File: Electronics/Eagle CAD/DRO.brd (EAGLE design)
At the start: 52.1 x 98 mm, 40 parts, among them J1 USB_MINI-B-MICRO-B_FCI, J10 CONN-4-2.54X1-RA, J11 USB-A-SHIELD, J12 CONN-8-2.54X2, J13 CONN-10-ARM, J14 CONN-40, J2 DE-9F-V, J3 DE-9F-V, J4 DE-9F-V, J5 DE-9F-V, J6 CONN-14-BIDI, J7 CONN-14-BIDI, J8 CONN-14-BIDI, J9 CONN-14-BIDI, SW1 SWITCH-SPDT-MINI-RA-SHORT, U1 74LCX14, U2 MIC5504-3.3, U3 SAMD21J17D, U4 74LCX14

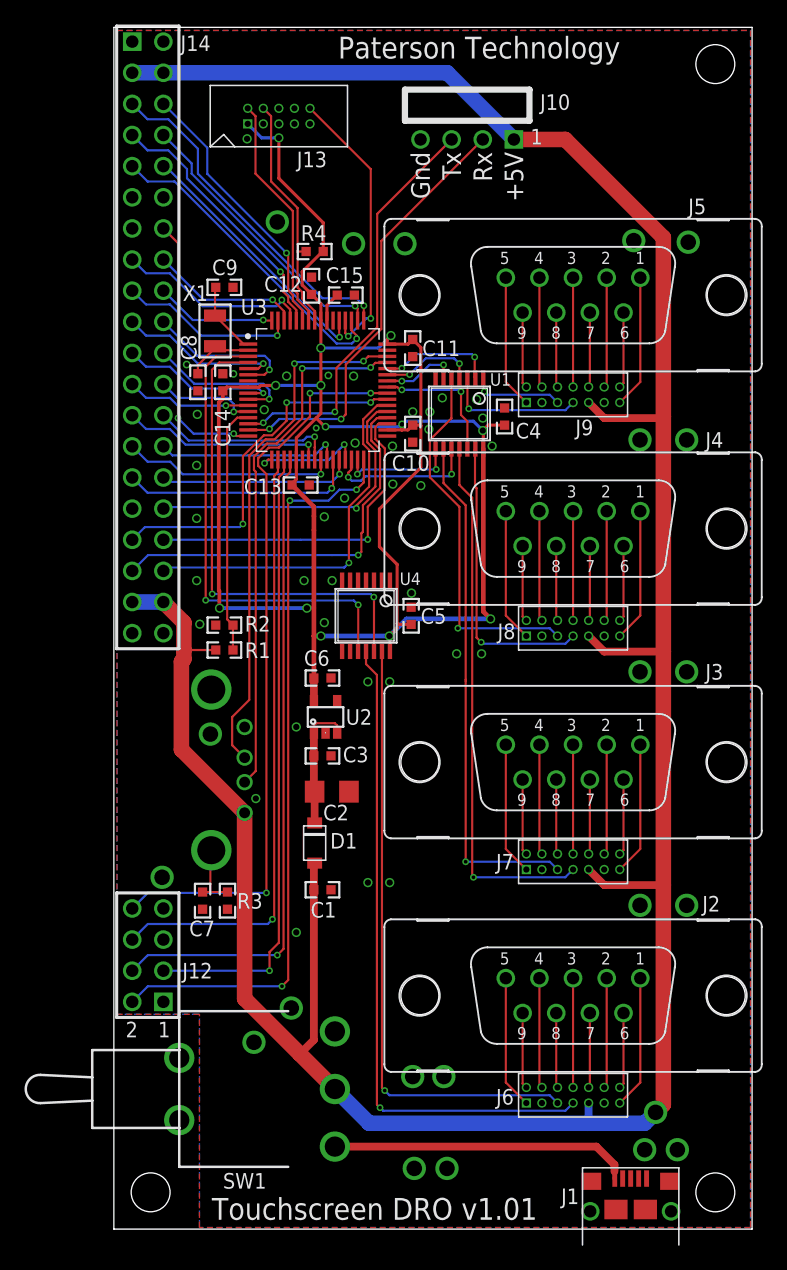
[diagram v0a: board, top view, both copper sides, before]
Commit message: Adjust certain holes sizes in PCB designs
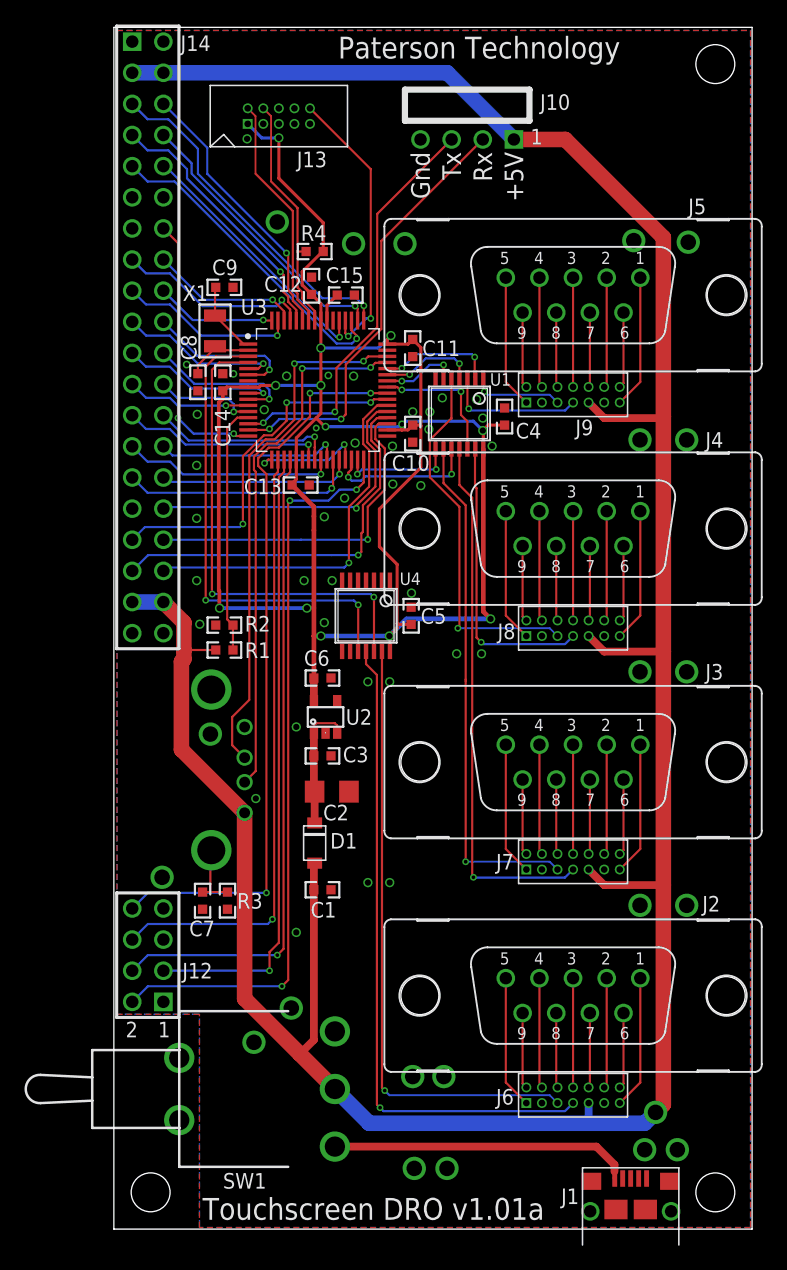
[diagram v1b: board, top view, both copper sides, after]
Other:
- board text added: "Touchscreen DRO v1.01a"
- board text removed: "Touchscreen DRO v1.01"
